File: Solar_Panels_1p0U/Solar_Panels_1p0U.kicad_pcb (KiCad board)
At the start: 2 copper layers, 92 x 82 mm, 46 parts, among them J1 5040500891

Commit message: 1.0U: Layout cells
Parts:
- removed D1, D10, D3, D5, D7, D9: D, Solar Panels Library:PMEG10020AELPX
- removed SC25, SC26, SC27: Solar_Cell, Solar Panels Library:Trisolx Wings
- added D11: PMEG3010EP, Solar Panel Library:PMEG10020AELPX, F.Cu at (169.9, 81.3)
- added J3: Conn_01x08_MountingPin, Connector_Molex:Molex_PicoBlade_53261-0871_1x08-1MP_P1.25mm_Horizontal, F.Cu at (184.9, 114.6)
- added J4: Conn_01x02, Connector_PinHeader_2.54mm:PinHeader_2x01_P2.54mm_Vertical, F.Cu at (154.0, 79.0)
- added J5: Conn_01x08_MountingPin, Connector_Molex:Molex_Pico-Lock_504050-0891_1x08-1MP_P1.50mm_Horizontal, B.Cu at (182.8, 114.8)
- D2: value D -> PMEG3010EP; footprint Solar Panels Library:PMEG10020AELPX -> Solar Panel Library:PMEG10020AELPX
- D4, D6, D8: value D -> PMEG3010EP; footprint Solar Panels Library:PMEG10020AELPX -> Solar Panel Library:PMEG10020AELPX; moved to F.Cu
- J1: value 5040500891 -> Conn_01x08_MountingPin; footprint Solar Panels Library:CON_5040500891 -> Connector_Molex:Molex_PicoBlade_53261-0871_1x08-1MP_P1.25mm_Horizontal
- SC1, SC10, SC11, SC12, SC13, SC14, SC15, SC16, SC17, SC18, SC19, SC2, SC20, SC21, SC22, SC23, SC24, SC3, SC4, SC5, SC6, SC7, SC8, SC9: value Solar_Cell -> KXOB25-05X3F; footprint Solar Panels Library:Trisolx Wings -> Solar Panel Library:KXOB25-05X3F
- moved D8 117.3 mm to (153.3, 151.6)
- moved JP3 113.5 mm to (166.9, 151.3), turned to 0 degrees
- moved H3 107.5 mm to (161.5, 151.2)
- moved D6 104.0 mm to (171.9, 130.1)
- moved SC22 101.1 mm to (137.8, 152.0)
- moved SC16 88.7 mm to (157.5, 131.4)
- moved D4 78.3 mm to (172.0, 108.5)
- moved SC21 77.9 mm to (157.5, 141.7), turned to 0 degrees
- moved SC19 70.9 mm to (105.5, 141.7), turned to 0 degrees
- moved SC10 62.7 mm to (157.5, 110.9)
- moved SC20 62.6 mm to (131.5, 141.7)
- moved SC23 60.9 mm to (112.0, 152.0), turned to 180 degrees
- moved SC15 60.0 mm to (157.5, 121.1), turned to 0 degrees
- moved SC1 55.2 mm to (87.5, 100.0), turned to 90 degrees
- moved SC9 50.6 mm to (157.5, 100.6), turned to 0 degrees
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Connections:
- SC1 pad 1: Net-(D1-A) -> Net-(SC1-+)
- SC12 pad 2: GND -> Net-(SC12--)
- SC13 pad 1: Net-(D5-A) -> Net-(SC13-+)
- SC18 pad 2: GND -> Net-(SC13-+)
- SC19 pad 1: Net-(D7-A) -> Net-(SC19-+)
- SC24 pad 2: GND -> Net-(SC19-+)
- SC6 pad 2: GND -> Net-(SC1-+)
- SC7 pad 1: Net-(D3-A) -> Net-(SC12--)
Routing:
- net Net-(D1-A): track 51.8 -> 0.00 mm
- net +VDC: track 43.7 -> 0.00 mm, vias 6 -> 0
- net Net-(SC4--): track 43.4 -> 0.00 mm
- net Net-(SC1--): track 41.6 -> 0.00 mm
- net Net-(SC25--): track 40.9 -> 0.00 mm
- net Net-(SC13--): track 40.7 -> 0.00 mm
- net Net-(SC19--): track 40.4 -> 0.00 mm
- net Net-(SC16--): track 40.4 -> 0.00 mm
- net Net-(SC7--): track 40.3 -> 0.00 mm
- net Net-(SC22--): track 40.2 -> 0.00 mm
- net Net-(SC10--): track 40.0 -> 0.00 mm
- net Net-(SC4-+): track 15.8 -> 0.00 mm
- net Net-(SC26--): track 15.3 -> 0.00 mm
- net Net-(SC23--): track 15.3 -> 0.00 mm
- net Net-(SC20--): track 15.1 -> 0.00 mm
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- added copper zone on F.Cu, net GND
- removed copper zone on F.Cu, net +VDC
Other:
- board text added: "+"
- board text added: "-"
- board text added: "CTS-SAT-1 | FrontierSat 1.25U Solar Panel Rev 2"
- board text added: "Spare DNP"
- board text added: "Stackup: 2 layers. 1.6mm FR4 PCB. All polygon pours: GND"
- board text added: "THIS SIDE IS NEGATIVE (orient toward MPI faceplate)"
- board text added: "THIS SIDE IS POSITIVE (orient away from MPI faceplate)"
- board text added: "This overlapping connector is intended to give the option between Microlock and Picoblade connectors."
- board text added: "pBlade|pLock"

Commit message: 1.0U: Finalize layout mostly
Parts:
- removed J3: Conn_01x08_MountingPin, Connector_Molex:Molex_PicoBlade_53261-0871_1x08-1MP_P1.25mm_Horizontal
- removed J4: Conn_01x02, Connector_PinHeader_2.54mm:PinHeader_2x01_P2.54mm_Vertical
- added D1: LED, LED_SMD:LED_0603_1608Metric_Pad1.05x0.95mm_HandSolder, F.Cu at (154.7, 150.8)
- added J2: PicoBlade_Vertical, Connector_Molex:Molex_PicoBlade_53047-0210_1x02_P1.25mm_Vertical, F.Cu at (87.0, 116.5)
- added J6: PicoBlade, Connector_Molex:Molex_PicoBlade_53261-0471_1x04-1MP_P1.25mm_Horizontal, B.Cu at (139.1, 132.1)
- added R1: 5k1, Resistor_SMD:R_0603_1608Metric_Pad0.98x0.95mm_HandSolder, B.Cu at (145.8, 133.4)
- D11, D2, D4, D6, D8: moved to B.Cu
- moved D11 56.9 mm to (124.9, 116.1), turned to 90 degrees
- moved J1 45.9 mm to (139.0, 115.6)
- moved J5 45.9 mm to (136.9, 115.8)
- moved D2 24.7 mm to (150.1, 102.7), turned to 180 degrees
- moved D6 23.8 mm to (150.1, 120.6), turned to 180 degrees
- moved D8 22.2 mm to (150.1, 129.6), turned to 180 degrees
- moved D4 22.1 mm to (150.1, 111.7), turned to 180 degrees
- moved SC1 2.00 mm to (87.5, 98.0)
- moved SC24 2.00 mm to (87.5, 134.0)
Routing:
- net Net-(JP2-A): track 0.00 -> 6.01 mm
- net Net-(JP1-A): track 0.00 -> 4.97 mm
- net Net-(JP3-A): track 0.00 -> 4.77 mm
- net Net-(J6-Pin_3): track 0.00 -> 4.72 mm
- net Net-(JP4-A): track 0.00 -> 4.67 mm
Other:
- board text added: "RBF"
- board text removed: "+"
- board text removed: "-"

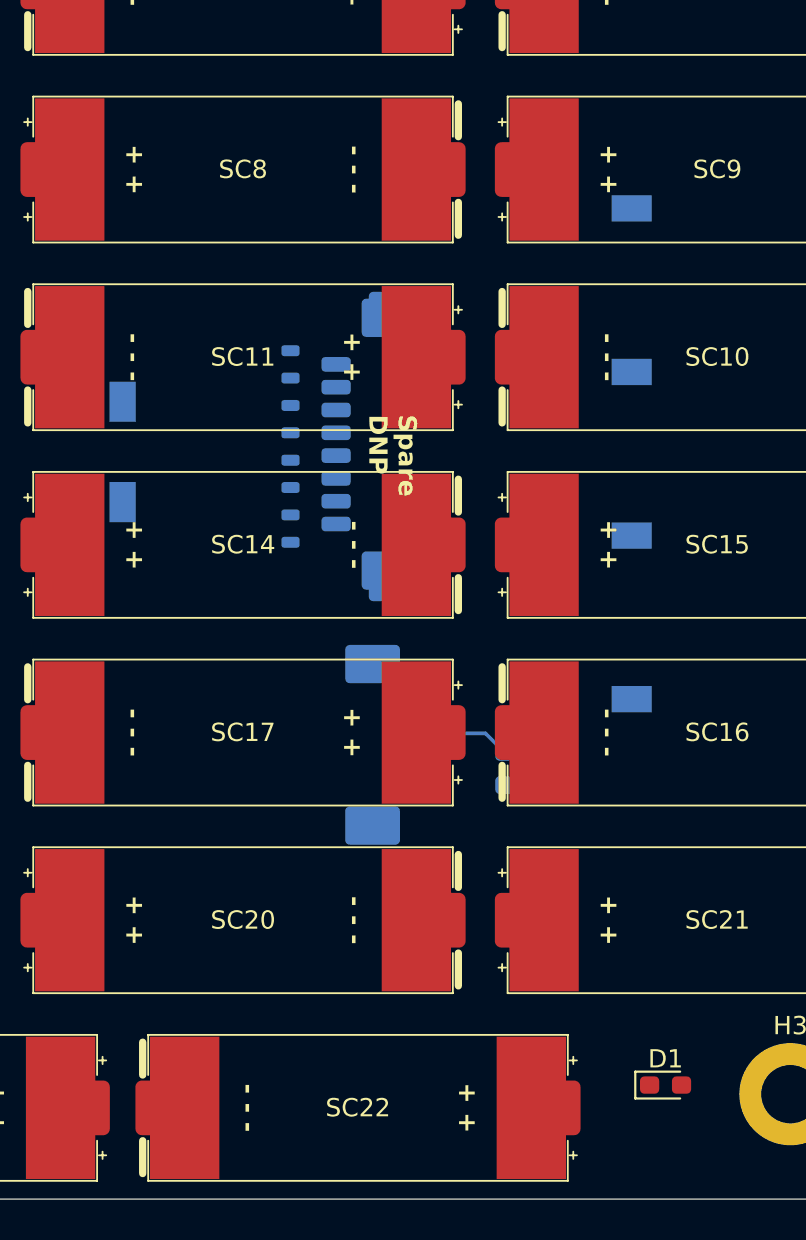
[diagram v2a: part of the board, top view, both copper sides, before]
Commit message: 1.0U: More layout and routing
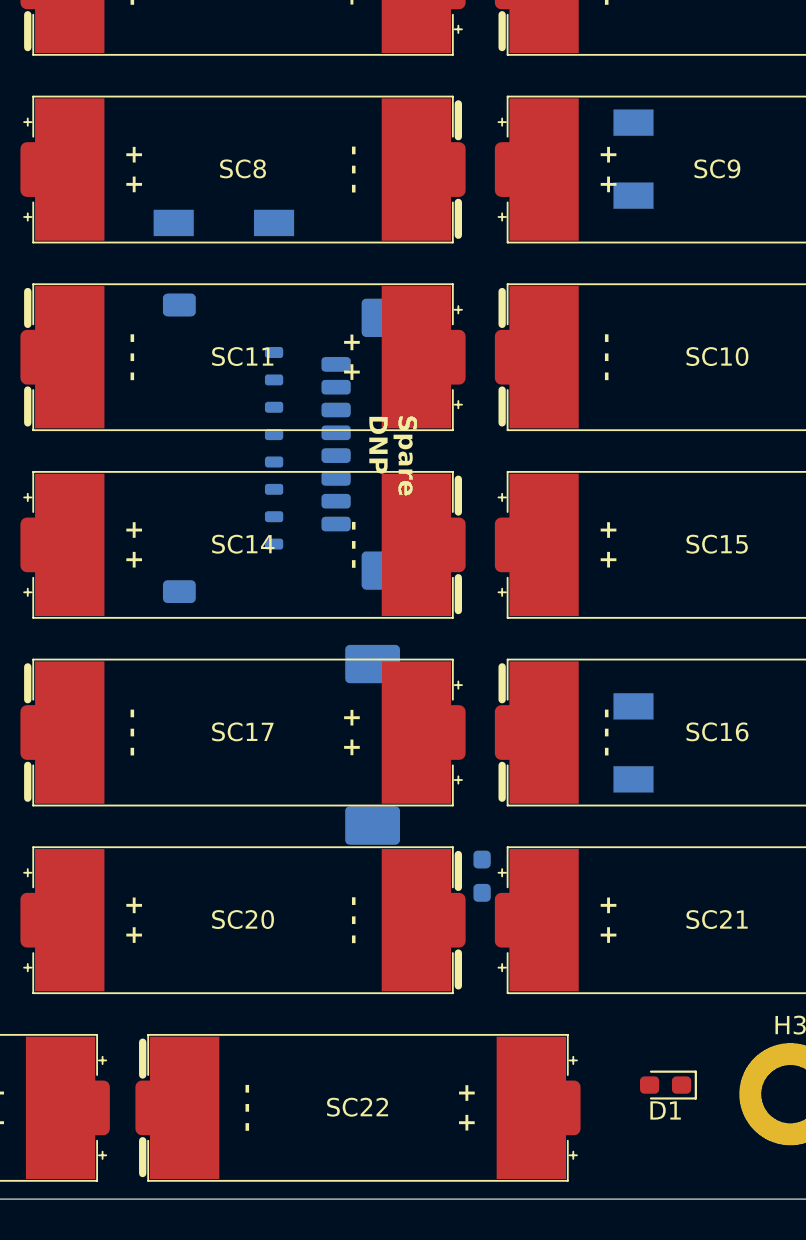
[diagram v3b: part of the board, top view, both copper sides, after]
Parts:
- moved D11 13.8 mm to (130.5, 103.5), turned to 180 degrees
- moved D4 9.67 mm to (150.1, 102.0), turned to 0 degrees
- moved D6 9.37 mm to (150.1, 130.0), turned to 0 degrees
- moved J5 6.49 mm to (130.4, 115.8), turned to 90 degrees
- moved R1 6.02 mm to (144.6, 139.3)
- moved D2 4.70 mm to (150.1, 98.0), turned to 0 degrees
- moved D8 4.40 mm to (150.1, 134.0), turned to 0 degrees
- turned D1 to 180 degrees
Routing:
- net Net-(J6-Pin_3): track 4.72 -> 0.00 mm

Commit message: Finish Rev 3 - 1.0U
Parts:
- moved R1 5.32 mm to (144.1, 134.0)
- moved J6 4.83 mm to (134.8, 130.0), turned to 180 degrees
- renumbered D1 to LED1
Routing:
- net +VDC: track 0.00 -> 67.8 mm
- net Net-(J2-Pin_1): track 0.00 -> 58.8 mm, vias 0 -> 1
- net Net-(J2-Pin_2): track 0.00 -> 55.8 mm, vias 0 -> 1
- net Net-(J6-Pin_4): track 0.00 -> 45.8 mm, vias 0 -> 1
- net Net-(LED1-A): track 0.00 -> 24.8 mm, vias 0 -> 1
- net Net-(SC1-+): track 0.00 -> 24.3 mm
- net Net-(SC19-+): track 0.00 -> 20.7 mm
- net Net-(SC22-+): track 0.00 -> 19.9 mm, vias 0 -> 1
- net Net-(SC4-+): track 0.00 -> 19.4 mm, vias 0 -> 1
- net Net-(SC10-+): track 0.00 -> 18.6 mm, vias 0 -> 1
- net Net-(SC23--): track 0.00 -> 18.5 mm
- net Net-(SC1--): track 0.00 -> 18.5 mm
- net Net-(J6-Pin_3): track 0.00 -> 16.3 mm
- net Net-(SC16-+): track 0.00 -> 14.7 mm, vias 0 -> 1
- net Net-(SC13-+): track 0.00 -> 10.3 mm
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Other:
- board text added: "CTS-SAT-1 | FrontierSat 1.0U Solar Panel Rev 3"
- board text added: "CTS-SAT-1 | FrontierSat | 1.0U Solar Panel | Rev 3"
- board text removed: "CTS-SAT-1 | FrontierSat 1.25U Solar Panel Rev 2"
- board text removed: "Spare DNP"
